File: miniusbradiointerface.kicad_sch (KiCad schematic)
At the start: 22 parts, among them J1 VCC, J2 DP, J3 DM, J4 GND, J5 DB9_Male, Q1 BSS138, U1 CM108AH, Y1 12M

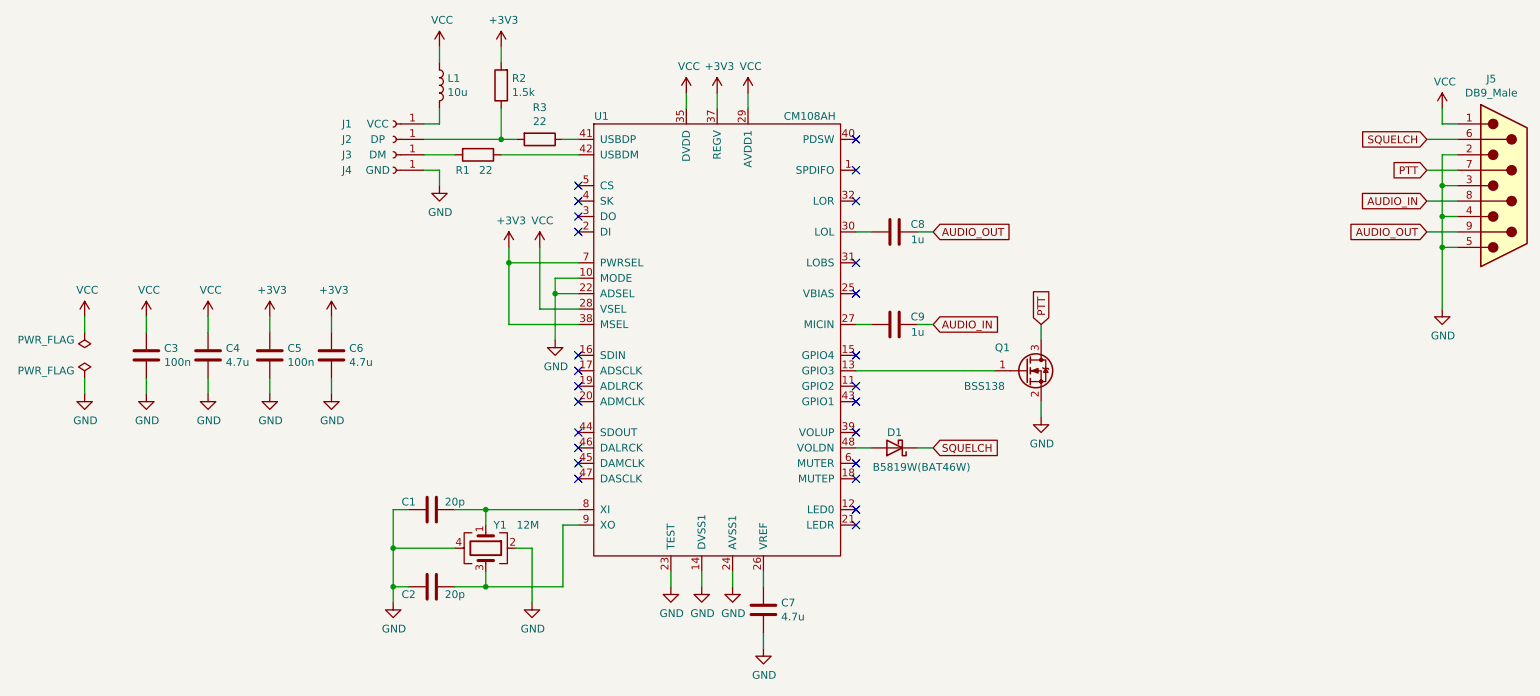
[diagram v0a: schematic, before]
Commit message: Update project to KiCad 8
Some symbols and footprints were updated and/or renamed in the library.
Update the symbols, keep the footprints. Fix ERC and DRC errors.
Update website URL and version
Update PDF schematic
Update ibom, add config file
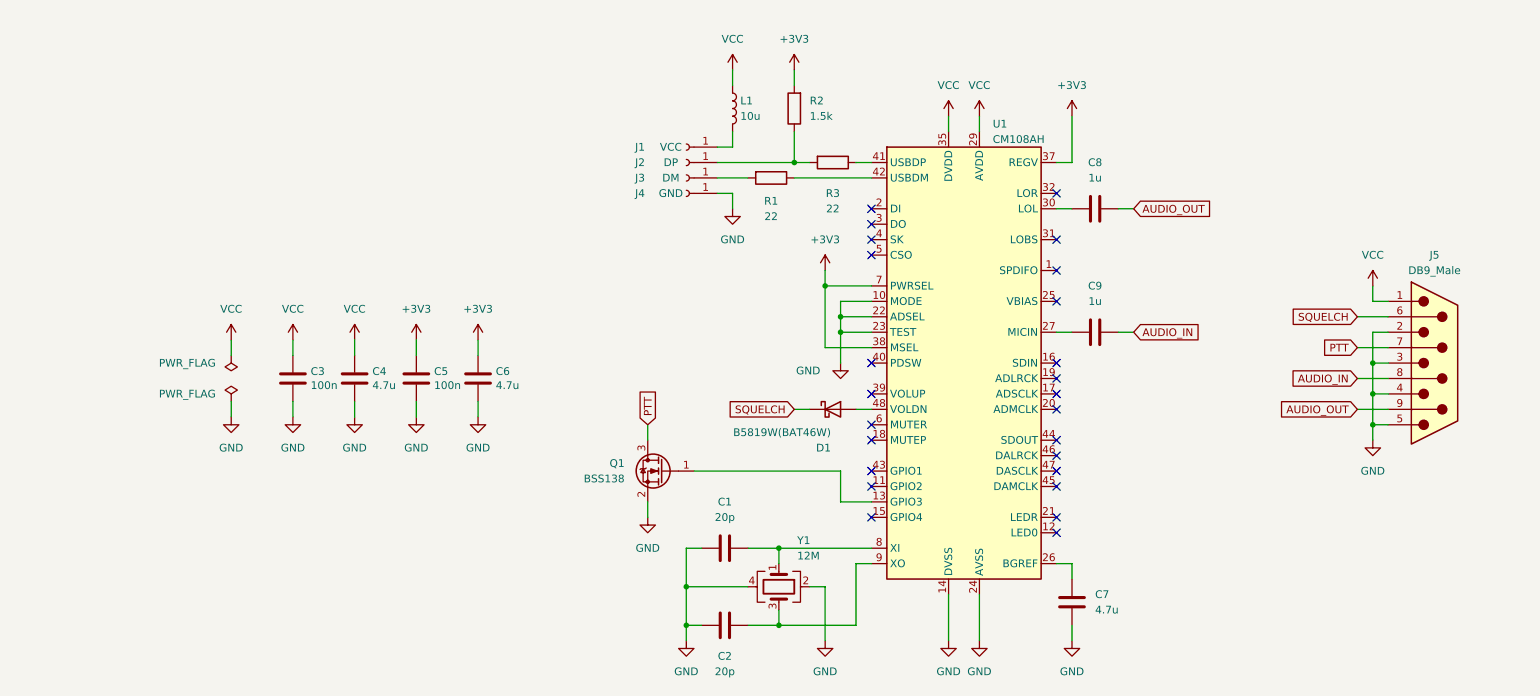
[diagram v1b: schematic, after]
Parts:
- removed U1: CM108AH, Package_QFP:LQFP-48_7x7mm_P0.5mm, symbol archive:Cmedia_USB_Audio_CM108AH
- added U1: CM108AH, Package_QFP:LQFP-48_7x7mm_P0.5mm, symbol Cmedia_USB_Audio:CM108AH
- J1, J2, J3, J4: symbol Connector:Conn_01x01_Female -> Connector:Conn_01x01_Socket
- J5: symbol Connector:DB9_Male -> Connector:DE9_Plug
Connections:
- net +3V3: now also U1.37 (REGV), U1.38 (MSEL), U1.7 (PWRSEL)
- net GND: now also U1.10 (MODE), U1.14 (DVSS), U1.22 (ADSEL), U1.23 (TEST), U1.24 (AVSS), U1.33 (AVSS), U1.36 (DVSS)
- net VCC: now also U1.29 (AVDD), U1.34 (AVDD), U1.35 (DVDD)
- net at Q1.1 (G): now also U1.13 (GPIO3)
- net at C7.1: now also U1.26 (BGREF)
- net at C9.2: now also U1.27 (MICIN)
- net at C8.2: now also U1.30 (LOL)
- net at R3.1: now also U1.41 (USBDP)
- net at R1.1: now also U1.42 (USBDM)
- net at D1.2 (A): now also U1.48 (VOLDN)
- net at C1.1, Y1.1: now also U1.8 (XI)
- net at C2.1, Y1.3: now also U1.9 (XO)
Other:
- moved on the sheet: C1, C2, C3, C4, C5, C6, C7, C8, C9, D1, J1, J2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
